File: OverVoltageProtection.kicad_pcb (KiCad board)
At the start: 2 copper layers, 67 x 42 mm, 36 parts, among them Q2 SQJQ466E, Q3 SQJQ466E, Q4 IRFR210PBF, U1 LM74800QDRRRQ1, U3 LM5069MM-2_NOPB

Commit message: Reworked schematics
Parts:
- removed C3: 1uF, Capacitor_SMD:C_1206_3216Metric
- removed D4: 1N4002, Diode_THT:D_DO-41_SOD81_P10.16mm_Horizontal
- removed Q4: IRFR210PBF, Package_TO_SOT_SMD:TO-252-3_TabPin2
- removed R3: 10k, Resistor_SMD:R_1206_3216Metric_Pad1.30x1.75mm_HandSolder
- removed U1: LM74800QDRRRQ1, LM74800QDRRRQ1:IC_LM74800QDRRRQ1
- added C7: 1uF, Capacitor_SMD:C_1206_3216Metric, F.Cu at (138.2, 67.2)
- added C8: 0.015uF, Capacitor_SMD:C_1206_3216Metric, F.Cu at (138.2, 70.5)
- added D6: 1N6263, Diode_THT:D_DO-35_SOD27_P7.62mm_Horizontal, F.Cu at (169.4, 74.0)
- added D8: 1N4002, Diode_THT:D_DO-41_SOD81_P10.16mm_Horizontal, F.Cu at (155.0, 79.3)
- added Q5: IRFR210PBF, Package_TO_SOT_SMD:TO-263-3_TabPin2, F.Cu at (163.9, 62.5)
- added R4: 10k, Resistor_SMD:R_1206_3216Metric_Pad1.30x1.75mm_HandSolder, F.Cu at (150.2, 37.6)
- added U2: LM74800QDRRRQ1, LM74800QDRRRQ1:IC_LM74800QDRRRQ1, F.Cu at (174.5, 53.8)
- C4: value 100nF -> 1uF
- D3: value 1N6263 -> BAV20
- Q2, Q3: value SQJQ466E -> SQJQ480E
- R6: value 3.48K -> 2.55K
- moved D1 108.5 mm to (169.0, 39.9)
- moved D2 108.5 mm to (169.0, 47.6)
- moved D3 103.0 mm to (169.4, 70.4), turned to 0 degrees
- moved C10 99.3 mm to (149.4, 69.5), turned to 0 degrees
- moved C9 97.7 mm to (149.4, 66.5), turned to 0 degrees
- moved R6 95.1 mm to (150.2, 44.2), turned to 0 degrees
- moved D7 92.8 mm to (169.4, 77.5), turned to 0 degrees
- moved R5 91.2 mm to (150.2, 40.9), turned to 0 degrees
- moved U3 88.1 mm to (167.7, 53.8), turned to 0 degrees
- moved C4 84.9 mm to (149.4, 60.5), turned to 0 degrees
- moved R11 83.8 mm to (150.2, 47.5), turned to 0 degrees
- moved Q2 81.7 mm to (158.4, 41.0), turned to 0 degrees
- moved Q3 80.9 mm to (158.4, 51.2), turned to 0 degrees
- moved C12 78.7 mm to (149.4, 72.5)
- moved R15 78.3 mm to (160.5, 73.2), turned to 0 degrees
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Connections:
- net Net-(R5--) renamed /OV
- C10 pad 2: GND -> GNDS
- C11 pad 2: GND -> GNDS
- C12 pad 2: GND -> GND1
- C13 pad 1: /V_INTER -> /VOUT_LM7480
- C13 pad 2: GND -> GNDS
- C14 pad 2: GND -> GND2
- C15 pad 1: /V_INTER -> /VOUT_LM7480
- C15 pad 2: GND -> GND2
- C16 pad 2: GND -> GND2
- C17 pad 2: GND -> GNDS
- C18 pad 2: GND -> GNDS
- C2 pad 1: /V_INTER -> /VOUT_LM7480
- C2 pad 2: GND -> GNDS
- C5 pad 1: /V_INTER -> /VOUT_LM7480
- C5 pad 2: GND -> GNDS
- C9 pad 2: GND -> GNDS
- D2 pad 1: GND -> GNDS
- D3 pad 1: /VS -> GNDS
- D3 pad 2: GND -> GND2
- D7 pad 2: GND -> GND2
- H1 pad 1: GND -> GNDS
- Q2 pad 1: /DGATE -> Net-(D7-K)
- Q2 pad 2: /V_INTER -> V_FILTERED
- Q2 pad 3: /V_INTER -> V_FILTERED
- Q2 pad 4: /V_INTER -> V_FILTERED
- Q2 pad 5: /OUT -> /SENSE
- Q3 pad 1: Net-(D7-K) -> /DGATE
- Q3 pad 2: /SENSE -> /OUT
- Q3 pad 3: /SENSE -> /OUT
- Q3 pad 4: /SENSE -> /OUT
- Q3 pad 5: V_FILTERED -> /VOUT_LM7480
- R12 pad 1: /V_INTER -> /VOUT_LM7480
- R13 pad 2: GND -> GND2
- R14 pad 2: GND -> GND2
- R15 pad 1: /V_INTER -> /VOUT_LM7480
- R5 pad 1: V_FILTERED -> /VOUT_LM7480
- R6 pad 2: GND -> GND1
- U3 pad 2: /V_INTER -> /VOUT_LM7480
- U3 pad 4: GND -> GND2
- U3 pad 5: GND -> GND2
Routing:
- net V_FILTERED: track 103.8 -> 3.50 mm, vias 4 -> 0
- net Net-(D7-K): track 58.3 -> 0.00 mm, vias 2 -> 0
- net /V_INTER: track 56.3 -> 0.00 mm
- net /VS: track 53.4 -> 0.00 mm, vias 4 -> 0
- net /SENSE: track 51.2 -> 0.00 mm, vias 2 -> 0
- net VBat: track 41.6 -> 0.00 mm
- net /OUT: track 36.4 -> 0.00 mm, vias 2 -> 0
- net /DGATE: track 30.1 -> 0.00 mm, vias 2 -> 0
- net /HGATE: track 20.1 -> 0.00 mm, vias 2 -> 0
- net Net-(C11-+): track 11.9 -> 0.00 mm
- net /UVLO: track 8.67 -> 0.00 mm
- net /OV: track 7.88 -> 0.00 mm
- net Net-(C14-+): track 6.69 -> 0.00 mm
- net Net-(R14-+): track 2.97 -> 0.00 mm
- net Net-(C4--): track 2.35 -> 0.00 mm
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
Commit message: new layout
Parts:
- removed D3: BAV20, Diode_THT:D_DO-35_SOD27_P7.62mm_Horizontal
- removed D8: 1N4002, Diode_THT:D_DO-41_SOD81_P10.16mm_Horizontal
- added D4: MRA4003T3G, Diode_SMD:D_SMA, F.Cu at (66.0, 58.0)
- added D5: BAS20, Package_TO_SOT_SMD:SOT-23, F.Cu at (95.5, 64.6)
- D6, D7: footprint Diode_THT:D_DO-35_SOD27_P7.62mm_Horizontal -> Diode_SMD:D_SOD-123
- moved D1 120.3 mm to (49.0, 49.2)
- moved D2 120.3 mm to (49.0, 56.5)
- moved D6 112.5 mm to (58.0, 58.0), turned to -90 degrees
- moved Q5 103.8 mm to (61.8, 43.9), turned to 90 degrees
- moved U2 103.6 mm to (71.0, 59.0)
- moved C10 101.3 mm to (53.0, 38.5), turned to 90 degrees
- moved C9 99.4 mm to (53.0, 42.5), turned to -90 degrees
- moved C12 98.1 mm to (52.0, 61.0), turned to 180 degrees
- moved R11 95.2 mm to (55.5, 57.0), turned to -90 degrees
- moved C11 92.6 mm to (46.5, 61.0), turned to 180 degrees
- moved R4 89.5 mm to (63.0, 58.0), turned to -90 degrees
- moved R15 87.3 mm to (75.5, 53.0)
- moved Q3 86.2 mm to (72.8, 42.0), turned to 90 degrees
- moved C7 78.2 mm to (60.5, 58.0), turned to -90 degrees
- moved D7 76.3 mm to (96.0, 56.5), turned to 90 degrees
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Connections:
- net /DGATE renamed /Stage1/DGATE
- net /HGATE renamed /Stage1/HGATE
- net /OUT renamed /Stage1/OUT
- net /OV renamed /Stage1/OV
- net /SENSE renamed /Stage2/SENSE
- net /UVLO renamed /Stage2/UVLO
- net /VOUT_LM7480 renamed /Stage1/VOUT_LM7480
- net /VS renamed /Stage1/VS
- C10 pad 2: GNDS -> GND1
- C11 pad 2: GNDS -> GND1
- C13 pad 2: GNDS -> GND1
- C17 pad 2: GNDS -> GND1
- C18 pad 2: GNDS -> GND1
- C2 pad 2: GNDS -> GND1
- C5 pad 2: GNDS -> GND1
- C9 pad 2: GNDS -> GND1
- D2 pad 1: GNDS -> GND1
- H1 pad 1: GNDS -> GND1
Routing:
- net /Stage1/VOUT_LM7480: track 0.00 -> 62.1 mm
- net V_FILTERED: track 3.50 -> 44.5 mm
- net VBat: track 0.00 -> 36.3 mm
- net /Stage1/OUT: track 0.00 -> 35.2 mm, vias 0 -> 2
- net /Stage1/VS: track 0.00 -> 33.3 mm, vias 0 -> 2
- net /Stage1/HGATE: track 0.00 -> 29.7 mm, vias 0 -> 2
- net GND2: track 0.00 -> 25.2 mm
- net /Stage2/SENSE: track 0.00 -> 16.7 mm
- net Net-(D7-K): track 0.00 -> 15.5 mm
- net /Stage1/OV: track 0.00 -> 15.0 mm, vias 0 -> 2
- net Net-(C11-+): track 0.00 -> 13.5 mm
- net /Stage1/DGATE: track 0.00 -> 13.4 mm, vias 0 -> 2
- net /Stage2/UVLO: track 0.00 -> 7.68 mm
- net Net-(C12-+): track 0.00 -> 3.46 mm
- net Net-(R14-+): track 0.00 -> 2.85 mm
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- added copper zone on B.Cu, net GND1
- added copper zone on F.Cu, net GND1
- removed copper zone on B.Cu, net GND
- removed copper zone on F.Cu, net GND
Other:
- board size 67 x 42 mm -> 67 x 37.8 mm

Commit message: fixed drc
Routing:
- net GND2: track 25.2 -> 29.7 mm
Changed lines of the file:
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@@
+	)
+	(segment
+		(start 99.686 56.942073)
+		(end 98.092073 56.942073)
+		(width 0.2)
+		(layer "F.Cu")
+		(net 12)
 	)
 	(segment
@@
 		(start 94.529468 65.025)
 		(end 93 65.025)
+		(width 0.2)
+		(layer "F.Cu")
+		(net 12)
+	)
+	(segment
+		(start 98.092073 56.942073)
+		(end 96 54.85)
 		(width 0.2)
 		(layer "F.Cu")
@@
 		(min_thickness 0.25)
 		(filled_areas_thickness no)
-		(fill
+		(fill yes
 			(thermal_gap 0.5)
 			(thermal_bridge_width 0.5)

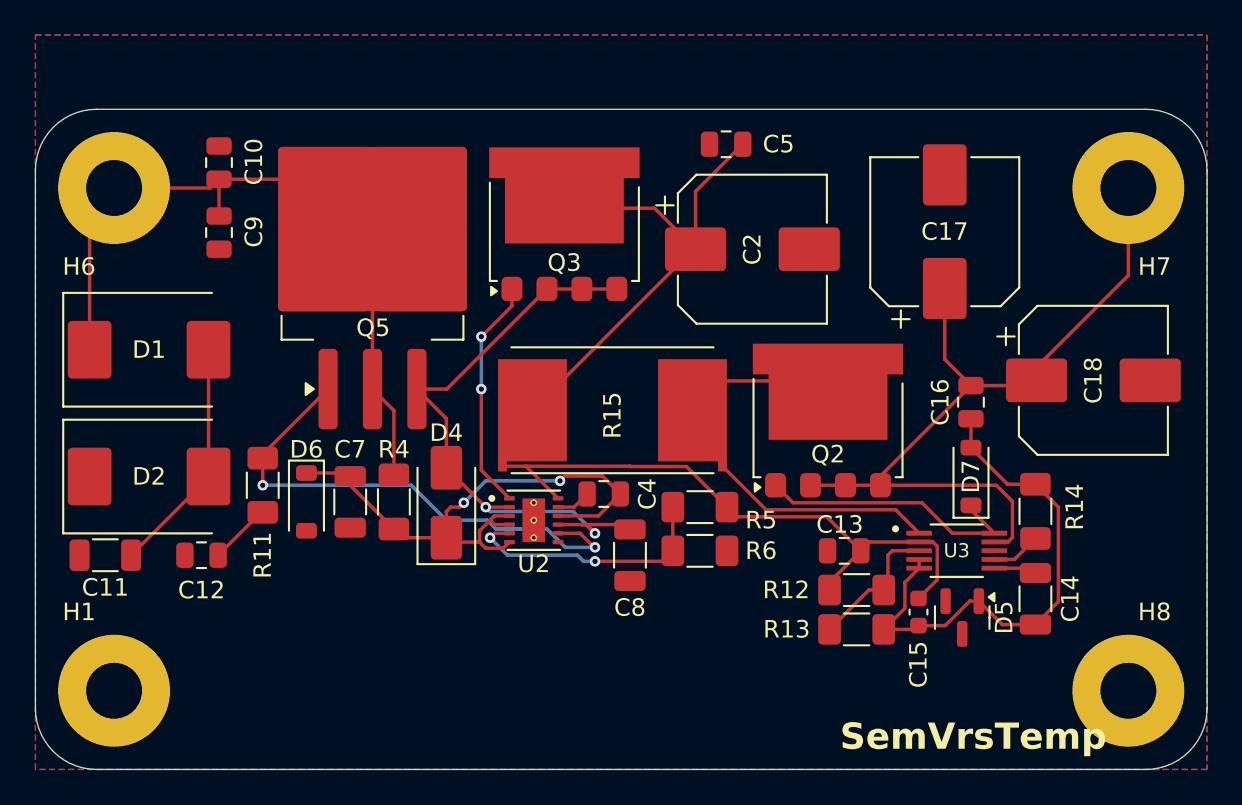
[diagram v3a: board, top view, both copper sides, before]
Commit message: updated trace with
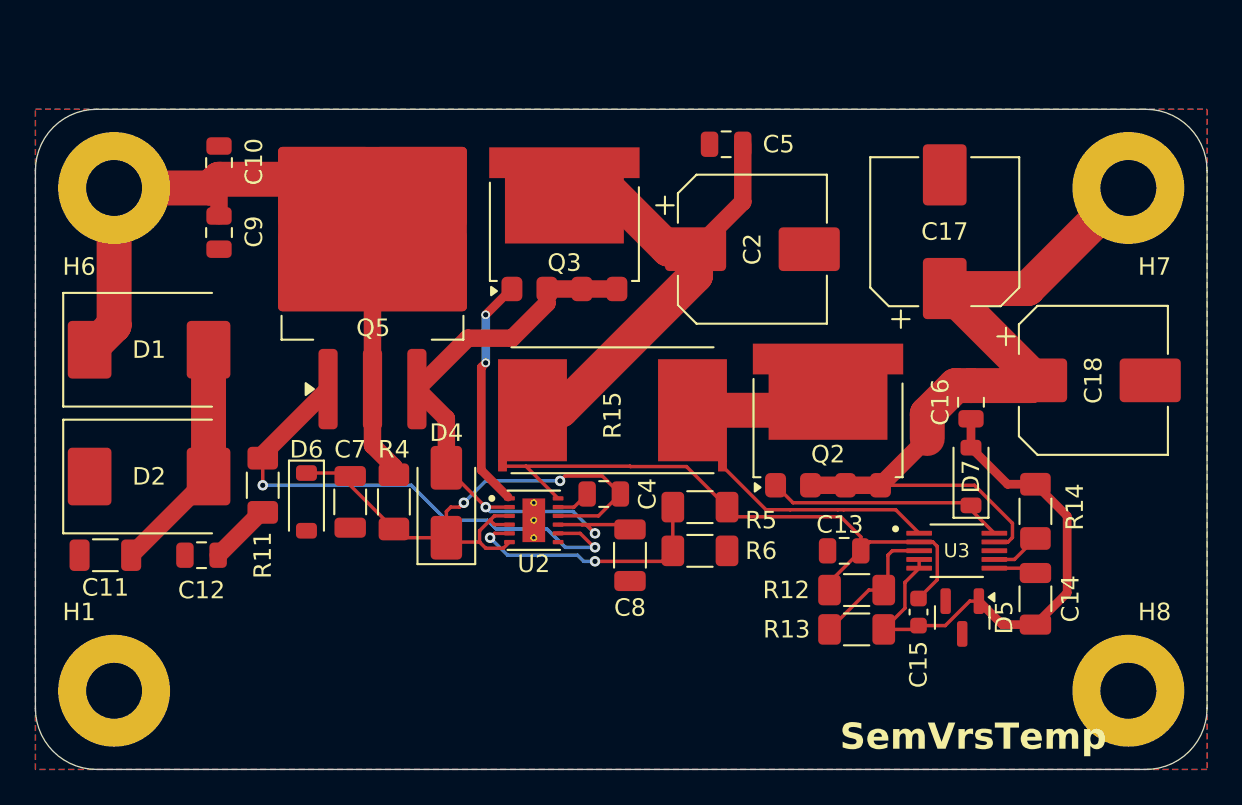
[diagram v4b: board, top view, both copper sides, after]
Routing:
- net /Stage2/SENSE: track 16.7 -> 20.7 mm
- net VBat: track 36.3 -> 38.9 mm
- net V_FILTERED: track 44.5 -> 46.9 mm
- net /Stage1/VOUT_LM7480: track 62.1 -> 64.1 mm
- net Net-(D7-K): track 15.5 -> 13.5 mm

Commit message: smal changes
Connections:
- C14 pad 2: GND2 -> GND1
- C15 pad 2: GND2 -> GND1
- C16 pad 2: GND2 -> GND1
- D5 pad 1: GND2 -> GND1
- D7 pad 2: GND2 -> GND1
- H8 pad 1: GND -> GND1
- R13 pad 2: GND2 -> GND1
- R14 pad 2: GND2 -> GND1
- U3 pad 4: GND2 -> GND1
- U3 pad 5: GND2 -> GND1
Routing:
- net GND2: track 30.2 -> 0.00 mm
- net GND1: track 0.00 -> 30.2 mm

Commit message: added via patches
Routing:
- net GND1: vias 0 -> 78

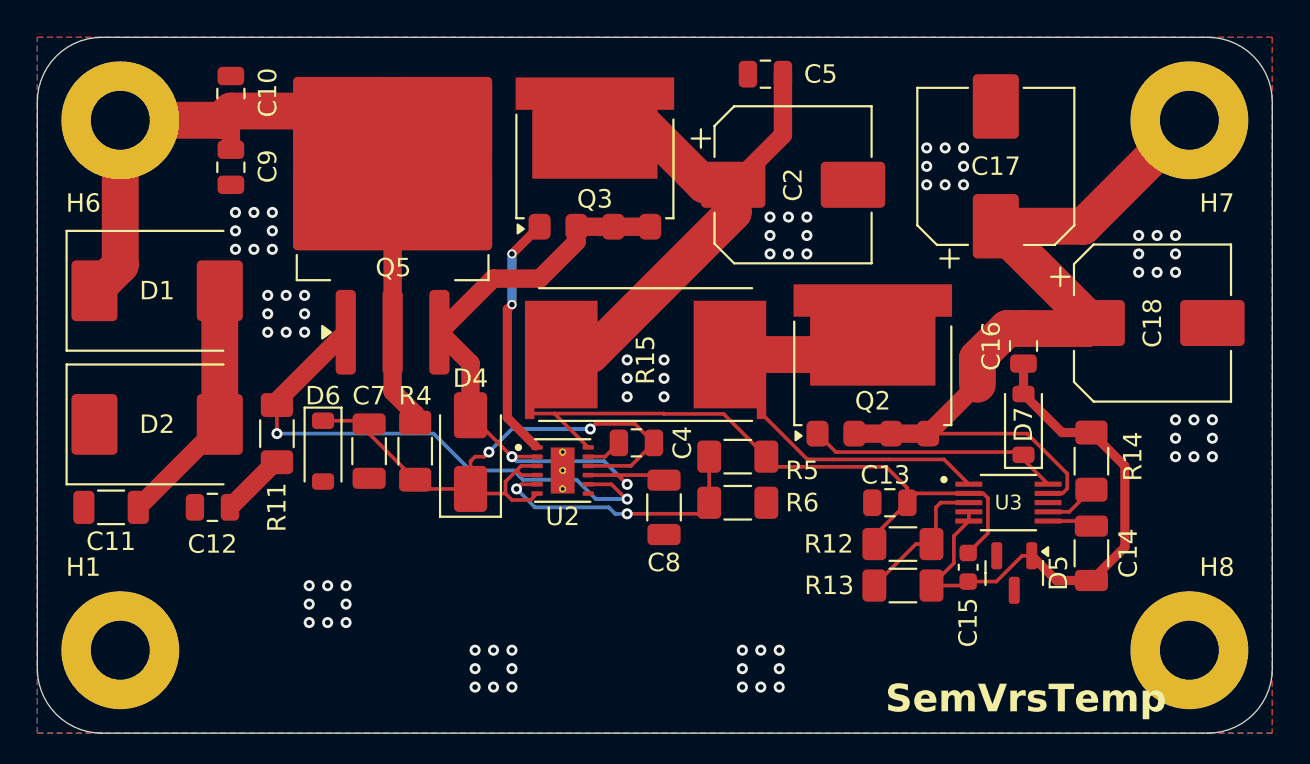
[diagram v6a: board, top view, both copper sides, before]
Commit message: updated layout
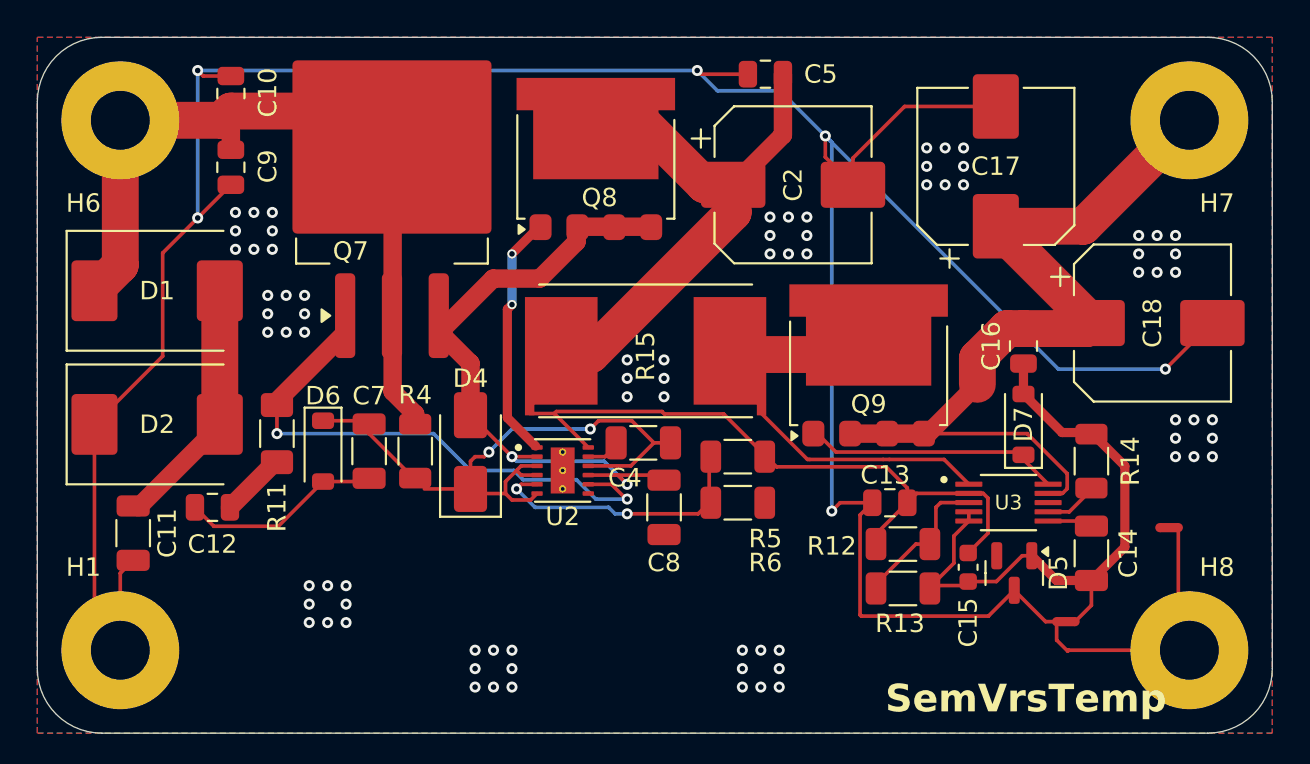
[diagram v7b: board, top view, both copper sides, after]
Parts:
- removed Q2, Q3: SQJQ480E, Package_TO_SOT_SMD:LFPAK88
- removed Q5: IRFR210PBF, Package_TO_SOT_SMD:TO-263-3_TabPin2
- added NT1: NetTie_2, NetTie:NetTie-2_SMD_Pad0.5mm, F.Cu at (103.9, 62.1)
- added NT2: NetTie_2, NetTie:NetTie-2_SMD_Pad0.5mm, F.Cu at (98.3, 67.2)
- added Q7: HUF76639S3ST, Package_TO_SOT_SMD:TO-263-3_TabPin2, F.Cu at (61.7, 43.0)
- added Q8: SQJQ466E-T1_GE3, Package_TO_SOT_SMD:LFPAK88, F.Cu at (72.8, 42.0)
- added Q9: SQJQ466E-T1_GE3, Package_TO_SOT_SMD:LFPAK88, F.Cu at (87.6, 53.2)
- C15: value 1000pF -> 1nF
- C4: footprint Capacitor_SMD:C_0805_2012Metric -> Capacitor_SMD:C_1206_3216Metric
- R12, R13, R14, R4, R5: footprint Resistor_SMD:R_1206_3216Metric_Pad1.30x1.75mm_HandSolder -> Resistor_SMD:R_1206_3216Metric
- R6: value 2.55K -> 2.55k; footprint Resistor_SMD:R_1206_3216Metric_Pad1.30x1.75mm_HandSolder -> Resistor_SMD:R_1206_3216Metric
- moved C11 1.84 mm to (47.7, 62.4), turned to -90 degrees
- moved C4 0.38 mm to (75.4, 57.5)
- moved R15 0.20 mm to (75.5, 52.8)
- moved R13 0.16 mm to (89.5, 65.4)
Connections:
- net /Stage1/OV renamed Net-(R5--)
- net /Stage1/VOUT_LM7480 renamed /Stage1/C
- C10 pad 2: GND1 -> GNDS
- C11 pad 2: GND1 -> GNDS
- C13 pad 2: GND1 -> GNDS
- C14 pad 2: GND1 -> GND2
- C15 pad 2: GND1 -> GND2
- C16 pad 2: GND1 -> GND2
- C17 pad 2: GND1 -> GNDS
- C18 pad 2: GND1 -> GNDS
- C2 pad 2: GND1 -> GNDS
- C5 pad 2: GND1 -> GNDS
- C9 pad 2: GND1 -> GNDS
- D2 pad 1: GND1 -> GNDS
- D5 pad 1: GND1 -> GND2
- D5 pad 3: GND1 -> GNDS
- D7 pad 2: GND1 -> GND2
- H1 pad 1: GND1 -> GNDS
- H8 pad 1: GND1 -> GNDS
- R13 pad 2: GND1 -> GND2
- R14 pad 2: GND1 -> GND2
- U3 pad 4: GND1 -> GND2
- U3 pad 5: GND1 -> GND2
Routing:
- net GNDS: track 0.00 -> 179.8 mm, vias 0 -> 6
- net GND2: track 0.00 -> 32.8 mm
- net GND1: track 30.2 -> 11.0 mm
- net /Stage1/VS: track 33.3 -> 34.1 mm
